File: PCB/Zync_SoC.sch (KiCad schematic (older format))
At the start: 7 parts

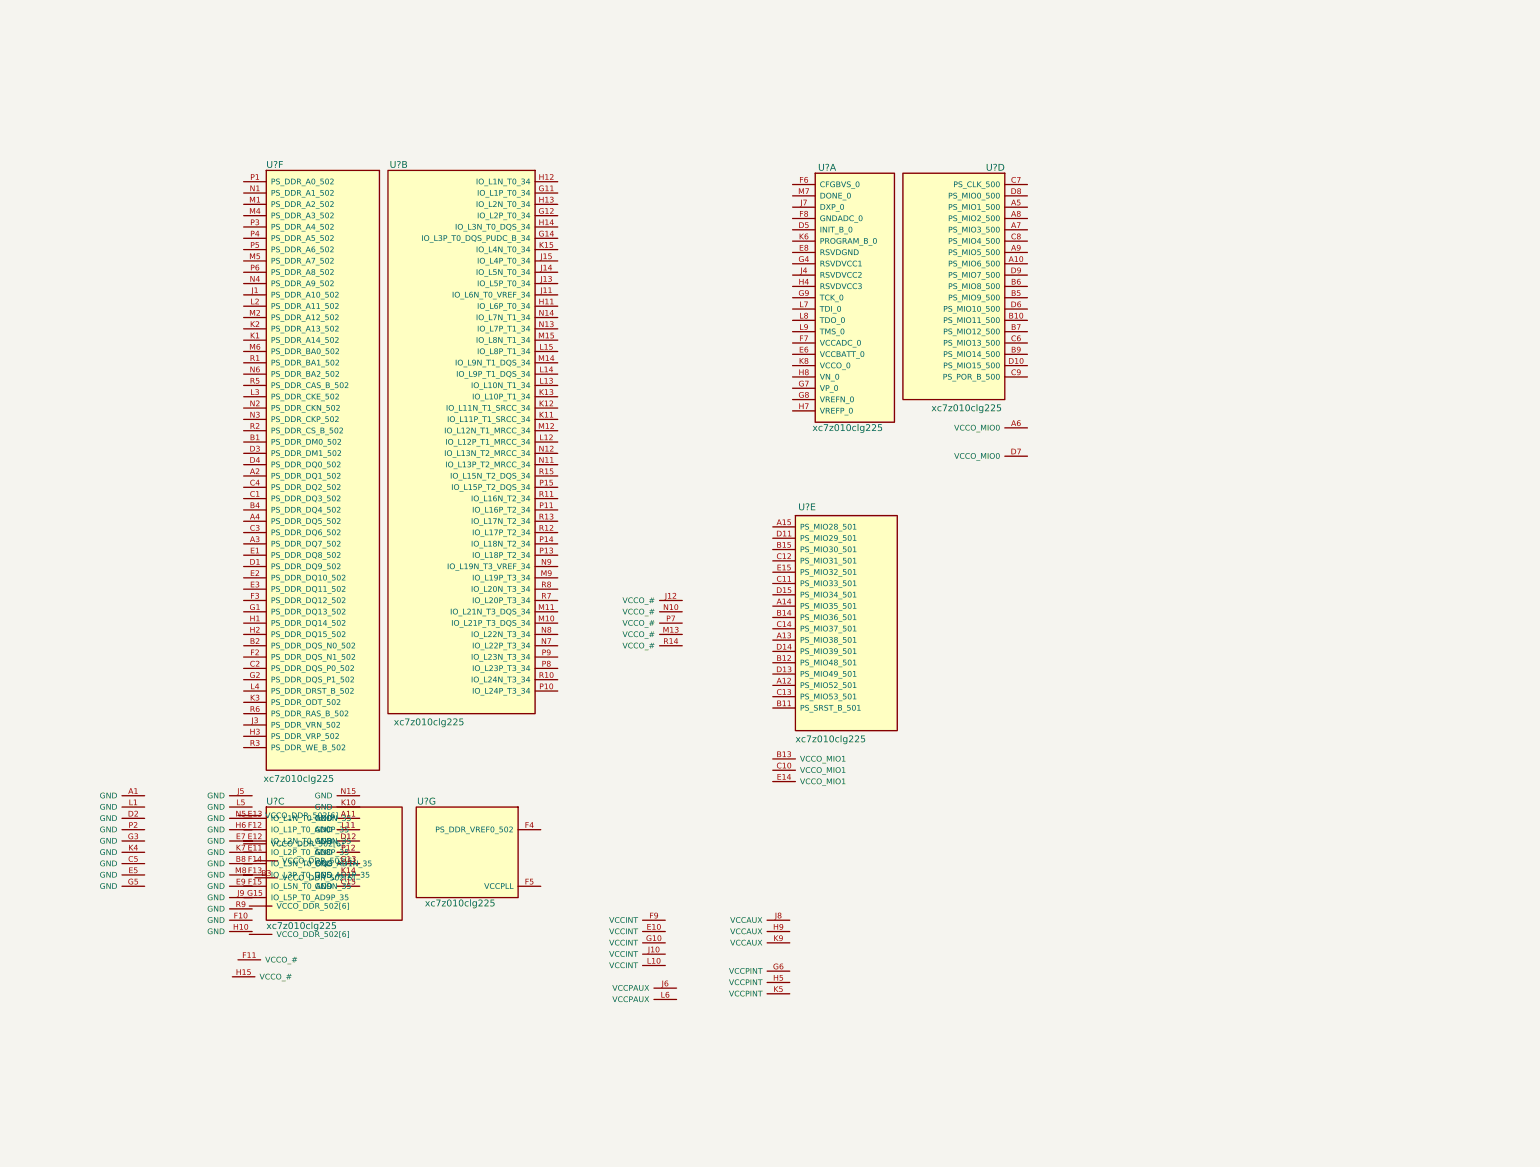
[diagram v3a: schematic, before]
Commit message: DDR3L
major progress on DDR3L schematic. Still need to edit bus enries and
make control signals their own entry each.
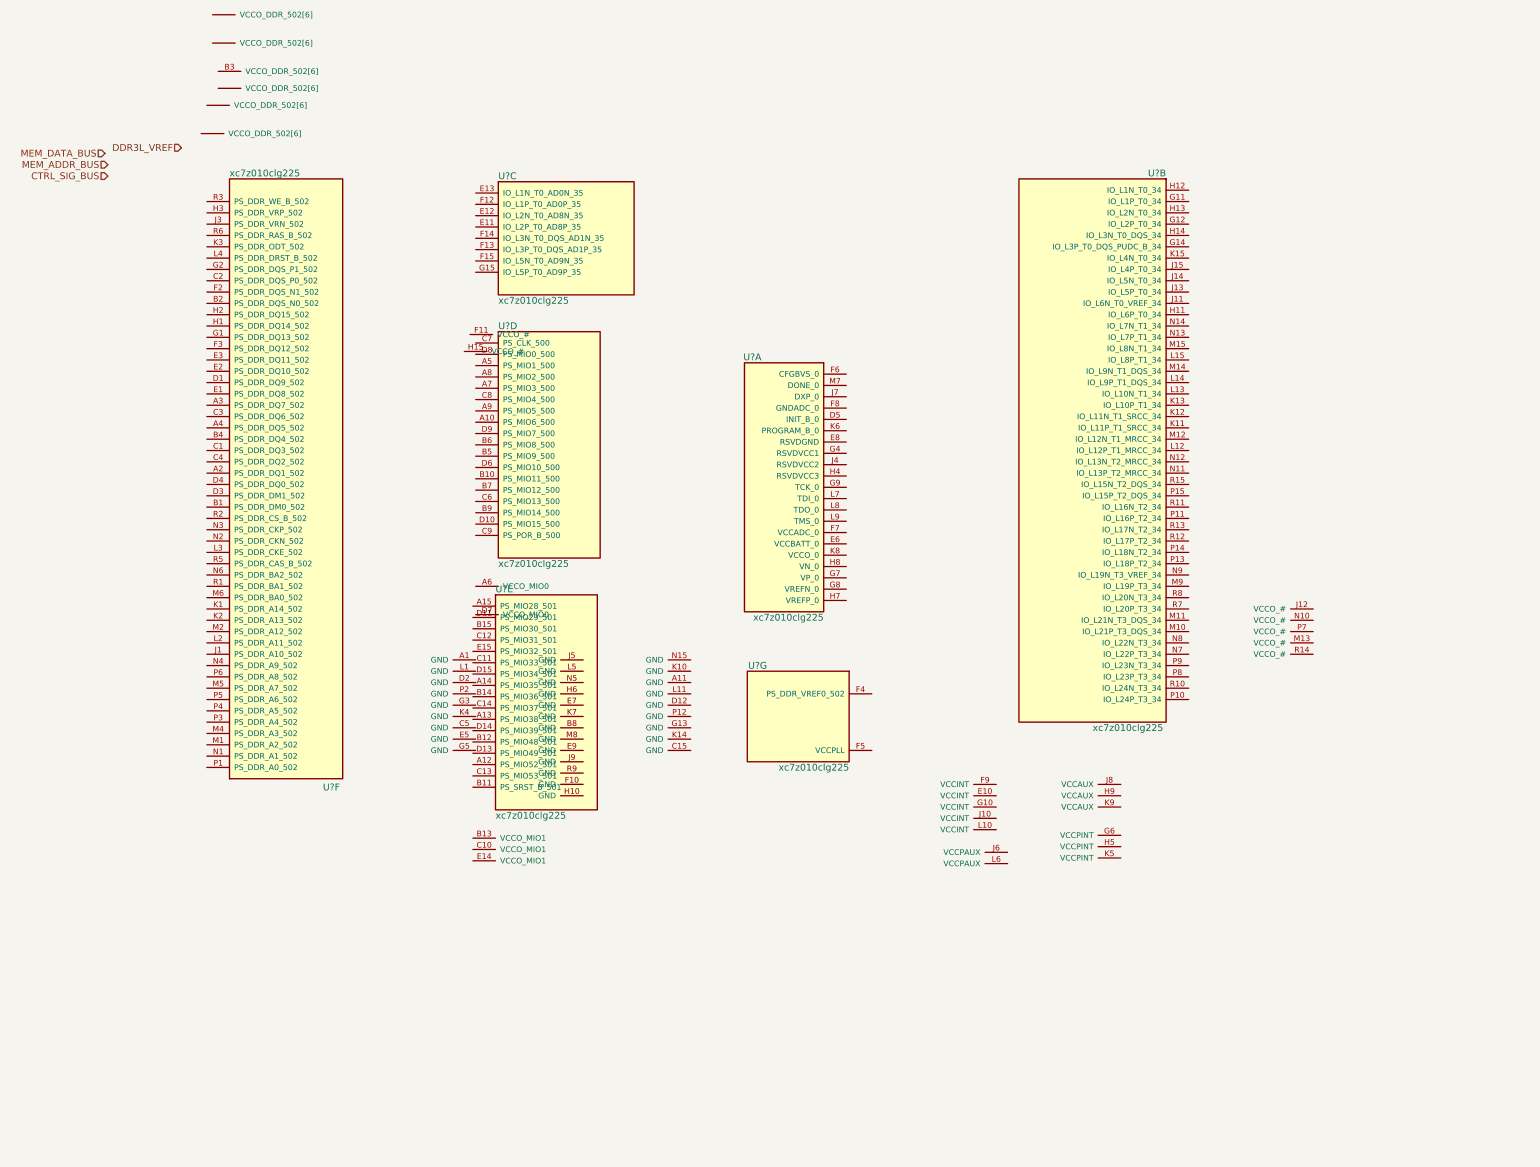
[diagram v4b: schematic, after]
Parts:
- removed U? (x7): xc7z010clg225, symbol xc7z010clg225
- added U? (x7): xc7z010clg225, PCB_Footprints:xc7z010clg225, symbol xc7z010clg225

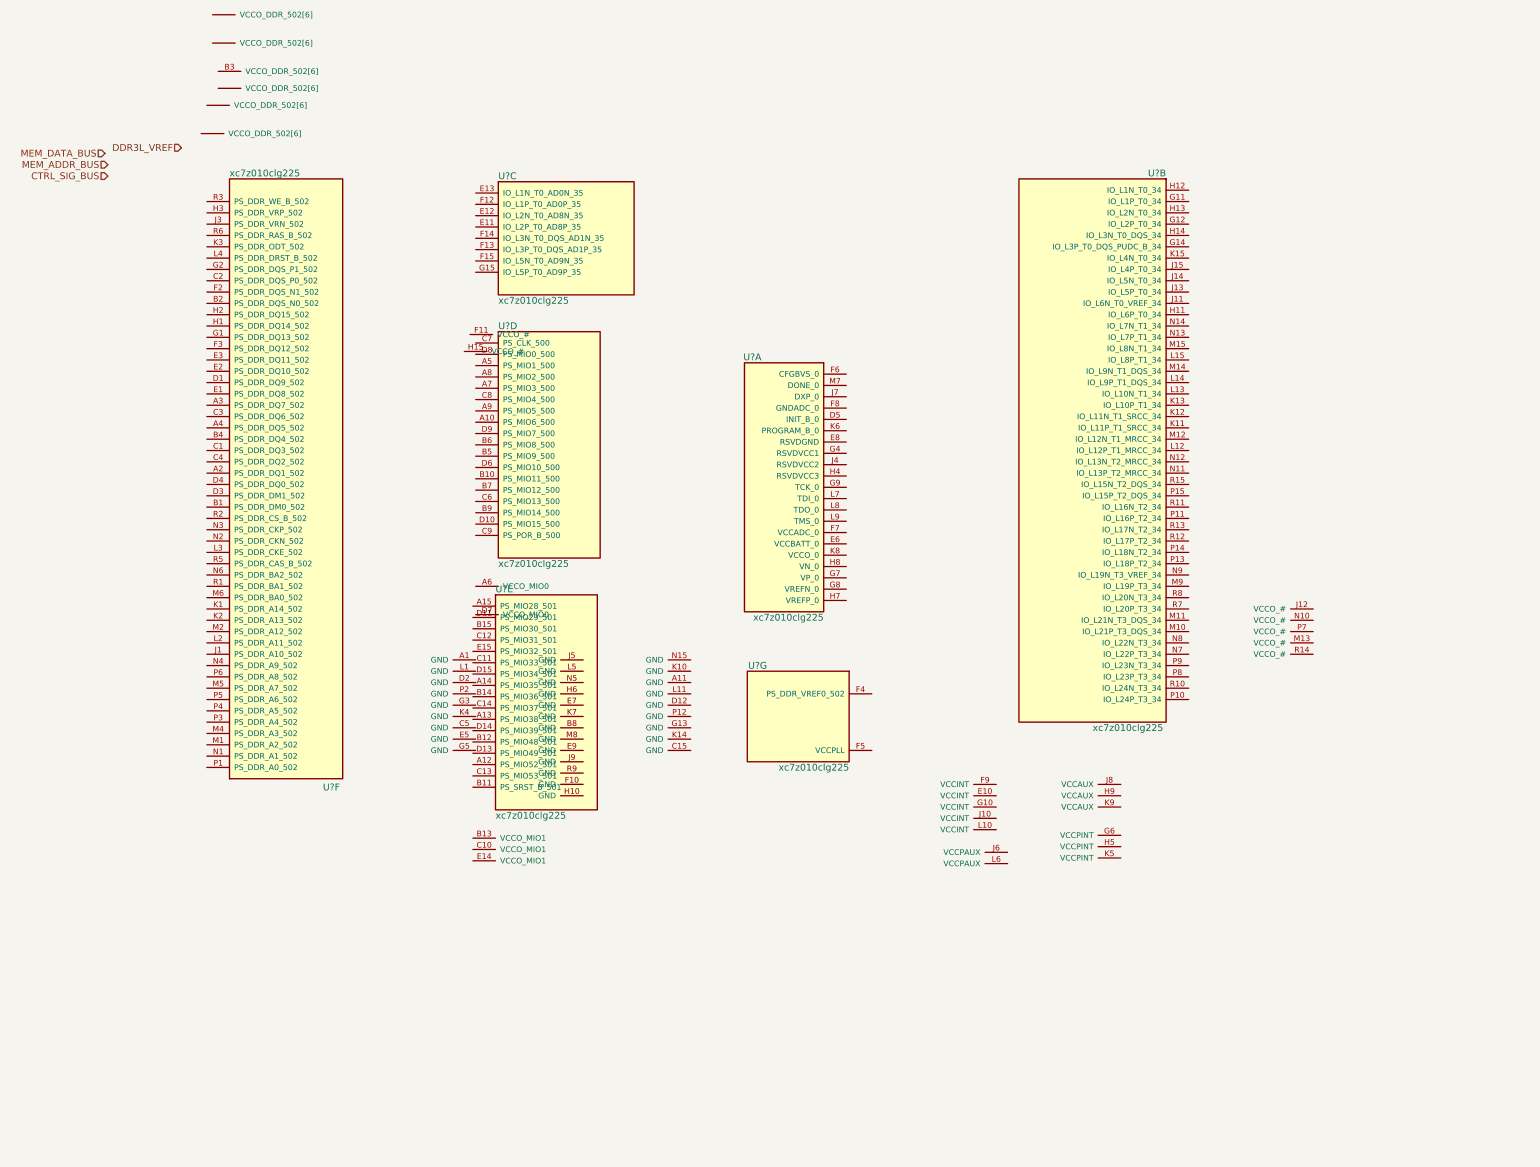
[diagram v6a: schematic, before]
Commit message: USB
This commit contains mostly work done to the USB sections. Theres a FTDI
chip for USB coms and programmign and an USB transceiver/PHY for usb
perfipherals or daisychaining devices.  Also the termiantion resistors
have been removed from the memory since termination can be set on DDR
pins of the FPGA with verilog.
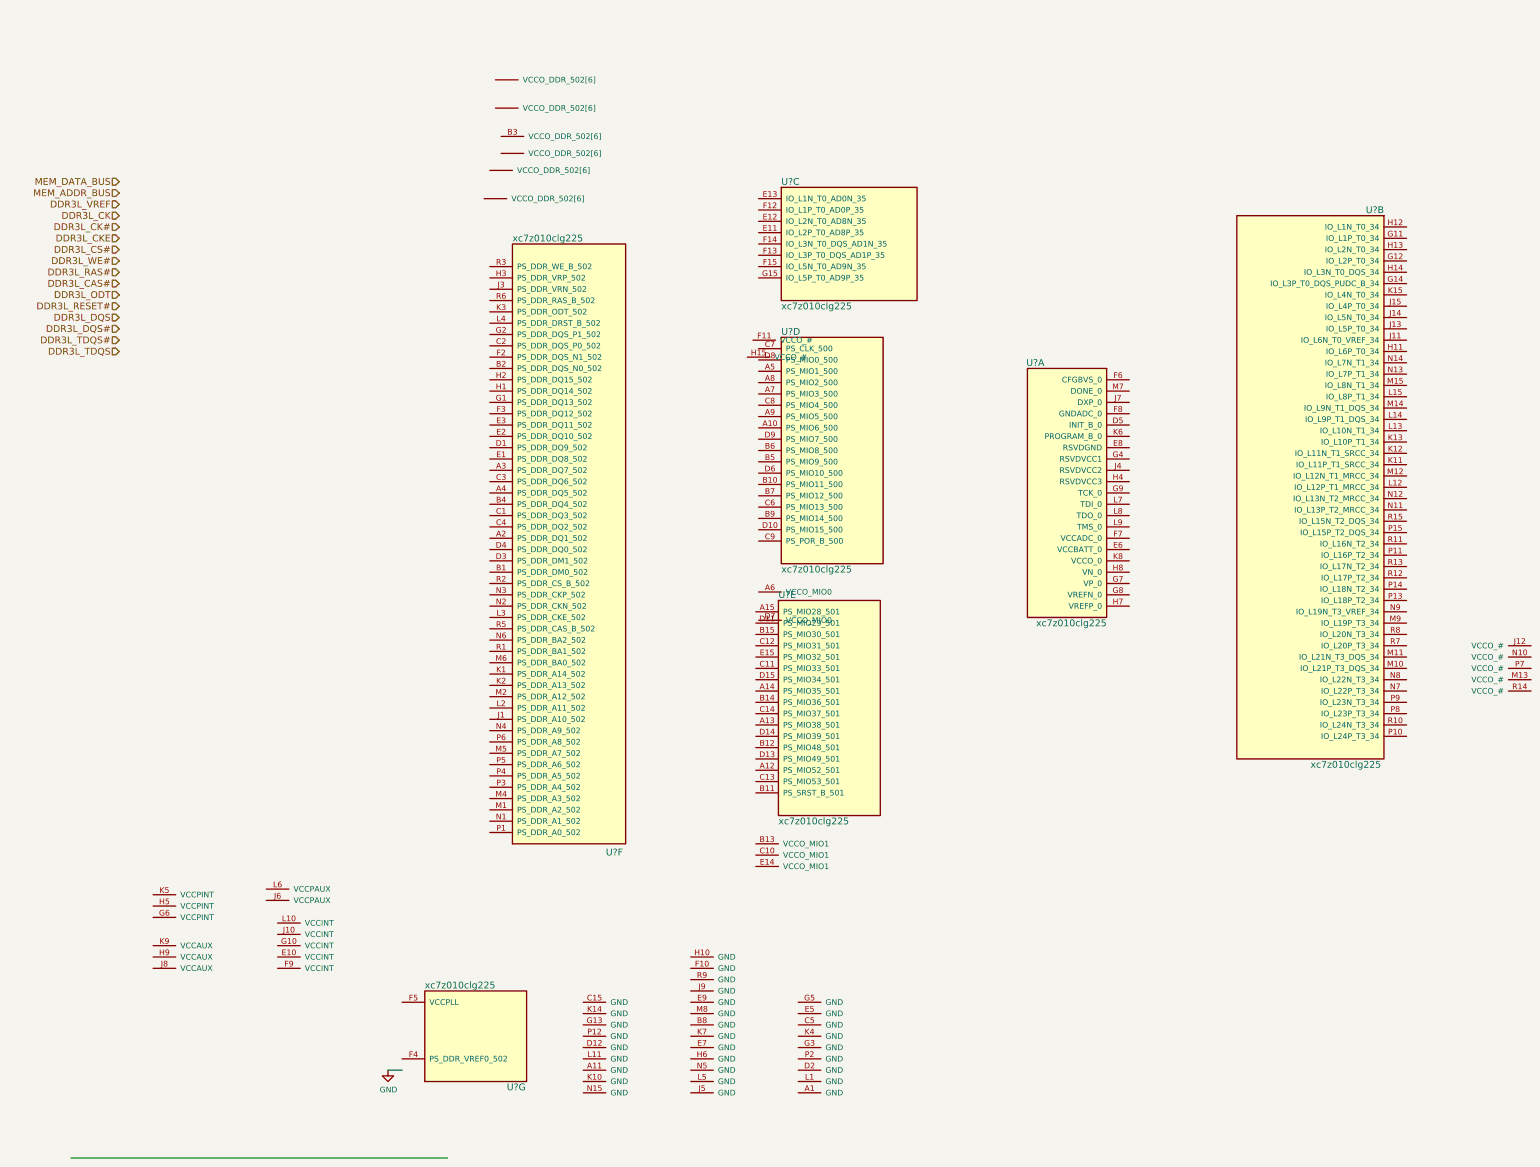
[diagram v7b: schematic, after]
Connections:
- net labels added: DDR3L_CAS#, DDR3L_CK, DDR3L_CK#, DDR3L_CKE, DDR3L_CS#, DDR3L_DQS, DDR3L_DQS#, DDR3L_ODT, DDR3L_RAS#, DDR3L_RESET#, DDR3L_TDQS, DDR3L_TDQS#, DDR3L_WE#, GND
- net labels removed: CTRL_SIG_BUS
- wire segments 0 -> 2
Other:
- moved on the sheet: U?A, U?B, U?C, U?D, U?E, U?F, U?G

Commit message: Power Topology change
Switching to a new PMIC TPS65400RGZR, has a much more compact PCB layout
and will provide all the necessary voltages for the system.
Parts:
- U? (x7): symbol xc7z010clg225 -> xc7z010clg225-RESCUE-ZyncMV
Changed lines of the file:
@@
 EESchema Schematic File Version 2
+LIBS:ZyncMV-rescue
 LIBS:power
 LIBS:device
@@
 $Descr B 17000 11000
 encoding utf-8
-Sheet 2 10
+Sheet 2 9
 Title ""
 Date "2016-12-23"
@@
 $EndDescr
 $Comp
-L xc7z010clg225 U?
+L xc7z010clg225-RESCUE-ZyncMV U?
 U 1 1 58785F37
 P 10300 2650
+AR Path="/58785F37" Ref="U?"  Part="1"
+AR Path="/585AE0B8/58785F37" Ref="U?"  Part="1"
 F 0 "U?" H 11050 2800 60  0000 L CNN
 F 1 "xc7z010clg225" H 10500 500 60  0000 L CNN
@@
 $EndComp
 $Comp
-L xc7z010clg225 U?
+L xc7z010clg225-RESCUE-ZyncMV U?
 U 2 1 58785FFF
 P 12750 1300
+AR Path="/58785FFF" Ref="U?"  Part="2"
+AR Path="/585AE0B8/58785FFF" Ref="U?"  Part="2"
 F 0 "U?" H 12950 1450 60  0000 L CNN
 F 1 "xc7z010clg225" H 12975 -3450 60  0000 L CNN
@@
 $EndComp
 $Comp
-L xc7z010clg225 U?
+L xc7z010clg225-RESCUE-ZyncMV U?
 U 3 1 587860DF
 P 7025 1050
+AR Path="/587860DF" Ref="U?"  Part="3"
+AR Path="/585AE0B8/587860DF" Ref="U?"  Part="3"
 F 0 "U?" H 7225 1200 60  0000 L CNN
 F 1 "xc7z010clg225" H 7225 100 60  0000 L CNN
@@
 $EndComp
 $Comp
-L xc7z010clg225 U?
+L xc7z010clg225-RESCUE-ZyncMV U?
 U 4 1 587861C9
 P 7025 2375
+AR Path="/587861C9" Ref="U?"  Part="4"
+AR Path="/585AE0B8/587861C9" Ref="U?"  Part="4"
 F 0 "U?" H 7225 2525 60  0000 L CNN
 F 1 "xc7z010clg225" H 7225 425 60  0000 L CNN
@@
 $EndComp
 $Comp
-L xc7z010clg225 U?
+L xc7z010clg225-RESCUE-ZyncMV U?
 U 5 1 58786297
 P 7000 4700
+AR Path="/58786297" Ref="U?"  Part="5"
+AR Path="/585AE0B8/58786297" Ref="U?"  Part="5"
 F 0 "U?" H 7200 4850 60  0000 L CNN
 F 1 "xc7z010clg225" H 7200 2850 60  0000 L CNN
@@
 $EndComp
 $Comp
-L xc7z010clg225 U?
+L xc7z010clg225-RESCUE-ZyncMV U?
 U 6 1 587863B3
 P 4650 6650
+AR Path="/587863B3" Ref="U?"  Part="6"
+AR Path="/585AE0B8/587863B3" Ref="U?"  Part="6"
 F 0 "U?" H 5675 6825 60  0000 L CNN
 F 1 "xc7z010clg225" H 4850 1400 60  0000 L CNN
@@
 $EndComp
 $Comp
-L xc7z010clg225 U?
+L xc7z010clg225-RESCUE-ZyncMV U?
 U 7 1 587864CB
 P 3875 8750
+AR Path="/587864CB" Ref="U?"  Part="7"
+AR Path="/585AE0B8/587864CB" Ref="U?"  Part="7"
 F 0 "U?" H 4800 8900 60  0000 L CNN
 F 1 "xc7z010clg225" H 4075 8000 60  0000 L CNN
